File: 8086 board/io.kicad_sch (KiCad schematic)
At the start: 63 parts, among them J3 RGB LCD, SW1 Q, SW10 A, SW11 S, SW12 D, SW13 F, SW14 G, SW15 H, SW16 J, SW17 O, SW18 P, SW19 Backspace, SW2 W, SW20 K, SW21 L, SW22 enter, SW23 M, SW24 space, SW25 alt, SW26 ctrl, SW27 Z, SW28 X, SW29 C, SW3 E, SW30 V, SW31 B, SW32 N, SW4 R, SW5 T, SW6 Y, SW7 U, SW8 I, SW9 shift, U13 74AC573, U14 74AC573, U15 74AC573, U16 74AC573, U17 74LVC245A, U18 74LVC245A, U19 74LVC245A, U2 74HC32

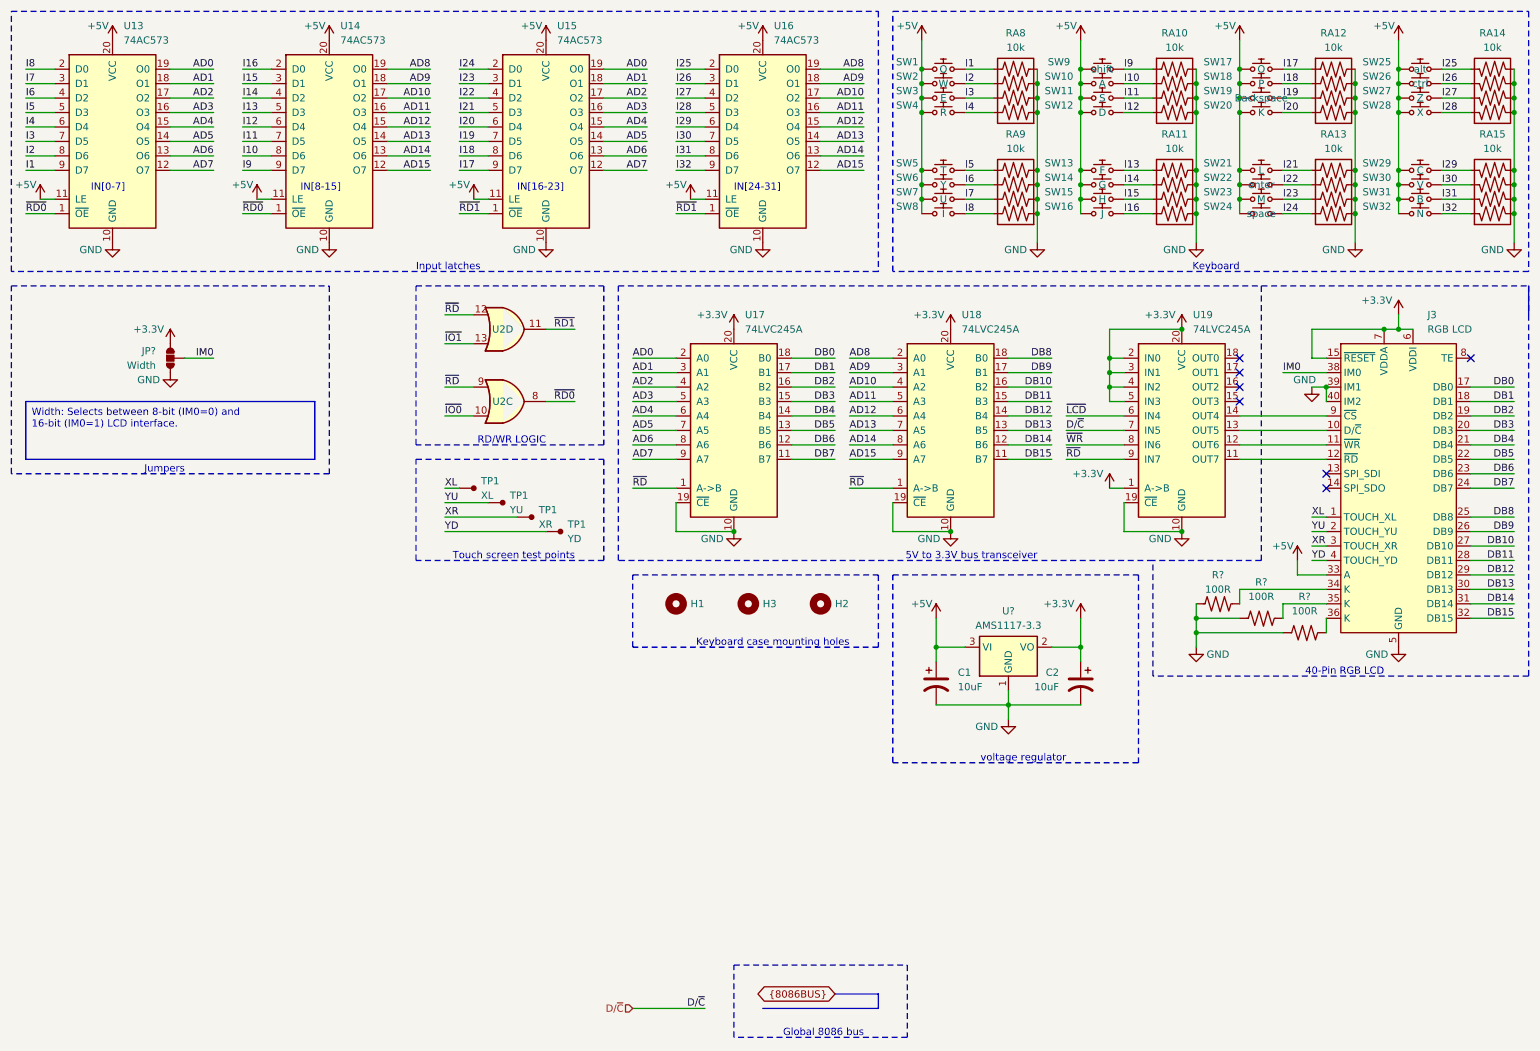
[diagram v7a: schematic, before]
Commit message: schematic: fix LCD RD bug, geographical reannotation
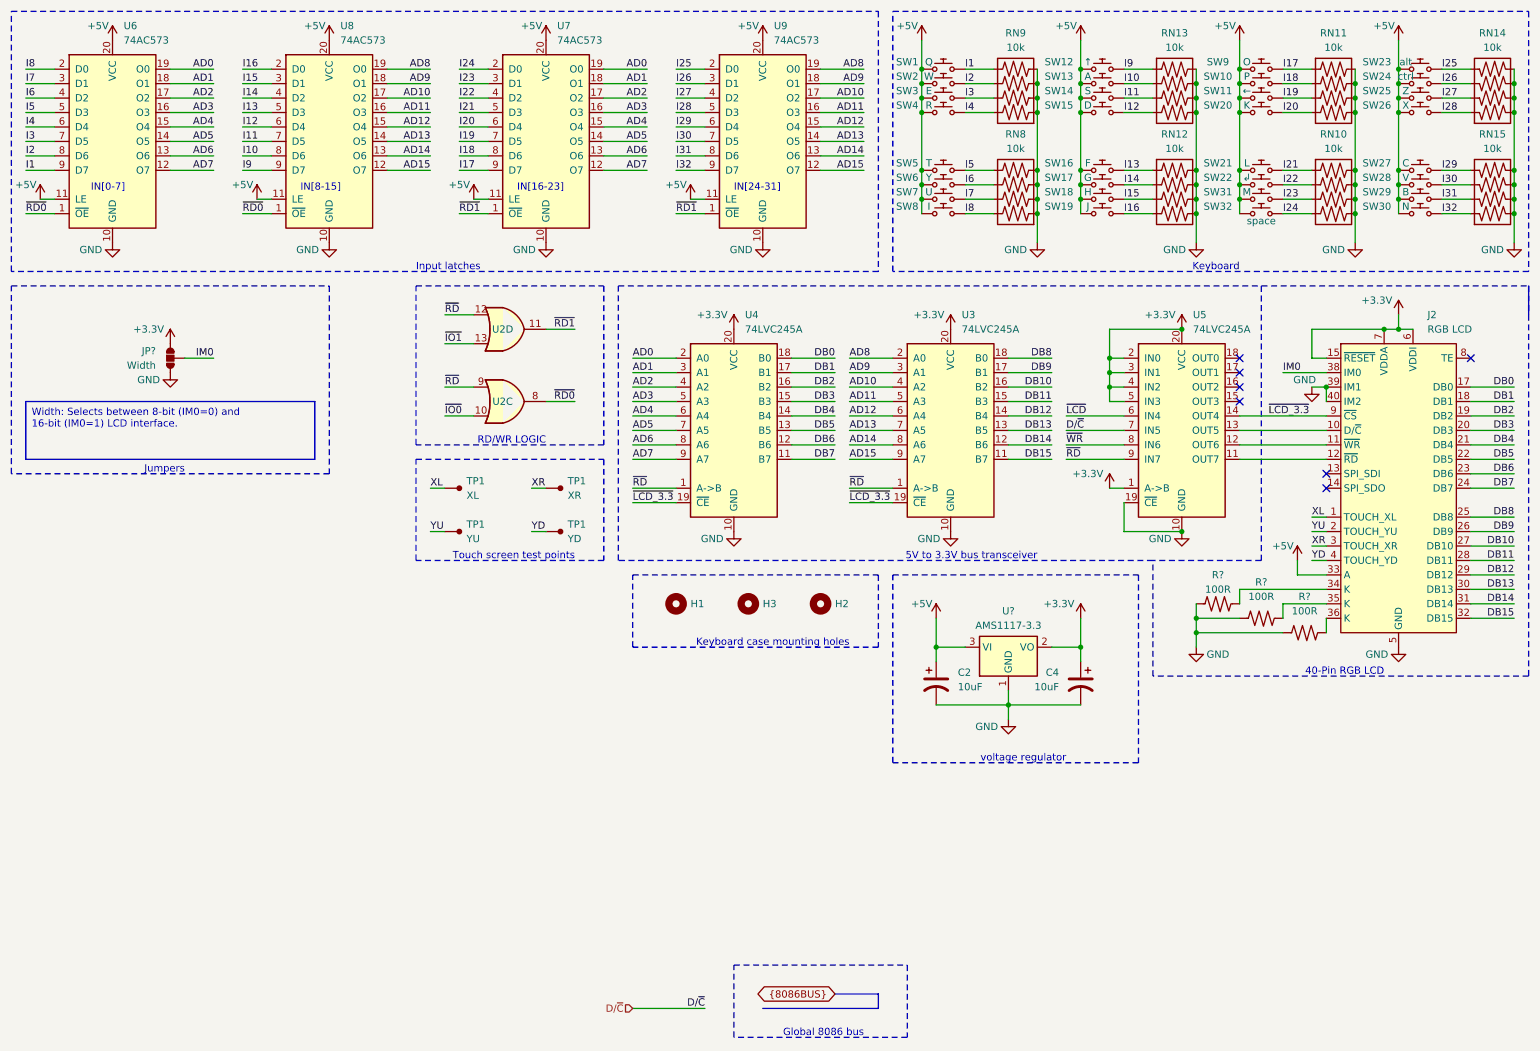
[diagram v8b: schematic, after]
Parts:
- H1, H2, H3, JP?: now left out of the parts list
- SW1: value Q -> ~; Key (none) -> Q
- SW10: renamed from SW18; value P -> ~; Key (none) -> P
- SW11: renamed from SW19; value Backspace -> ~; Key (none) -> ←
- SW12: renamed from SW9; value shift -> ~; Key (none) -> ↑
- SW13: renamed from SW10; value A -> ~; Key (none) -> A
- SW14: renamed from SW11; value S -> ~; Key (none) -> S
- SW15: renamed from SW12; value D -> ~; Key (none) -> D
- SW16: renamed from SW13; value F -> ~; Key (none) -> F
- SW17: renamed from SW14; value G -> ~; Key (none) -> G
- SW18: renamed from SW15; value H -> ~; Key (none) -> H
- SW19: renamed from SW16; value J -> ~; Key (none) -> J
- SW2: value W -> ~; Key (none) -> W
- SW20: value K -> ~; Key (none) -> K
- SW21: value L -> ~; Key (none) -> L
- SW22: value enter -> ~; Key (none) -> ↲
- SW23: renamed from SW25; value alt -> ~; Key (none) -> alt
- SW24: renamed from SW26; value ctrl -> ~; Key (none) -> ctrl
- SW25: renamed from SW27; value Z -> ~; Key (none) -> Z
- SW26: renamed from SW28; value X -> ~; Key (none) -> X
- SW27: renamed from SW29; value C -> ~; Key (none) -> C
- SW28: renamed from SW30; value V -> ~; Key (none) -> V
- SW29: renamed from SW31; value B -> ~; Key (none) -> B
- SW3: value E -> ~; Key (none) -> E
- SW30: renamed from SW32; value N -> ~; Key (none) -> N
- SW31: renamed from SW23; value M -> ~; Key (none) -> M
- SW32: renamed from SW24; value space -> ~; Key (none) -> space
- SW4: value R -> ~; Key (none) -> R
- SW5: value T -> ~; Key (none) -> T
- SW6: value Y -> ~; Key (none) -> Y
- SW7: value U -> ~; Key (none) -> U
- SW8: value I -> ~; Key (none) -> I
- SW9: renamed from SW17; value O -> ~; Key (none) -> O
- TP1: value XR -> ~; Signal (none) -> XR; now left out of the parts list
- TP1: value XL -> ~; Signal (none) -> XL; now left out of the parts list
- TP1: value YD -> ~; Signal (none) -> YD; now left out of the parts list
- TP1: value YU -> ~; Signal (none) -> YU; now left out of the parts list
- U2: now in the parts list
- renumbered C1 to C2, C2 to C4, J3 to J2, RA13 to RN10, RA12 to RN11, RA11 to RN12, RA10 to RN13, RA14 to RN14, RA15 to RN15, RA9 to RN8, RA8 to RN9, U18 to U3, U17 to U4, U19 to U5, U13 to U6, U15 to U7, U14 to U8, U16 to U9
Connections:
- net GND: no longer U3.19 (~{CE}), U4.19 (~{CE})
- net ~{LCD_3.3}: now reaches J2.9 (~{CS}), U5.14 (B4)
- net ~{LCD_3.3}: now also U3.19 (~{CE}), U4.19 (~{CE})
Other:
- moved on the sheet: TP1
